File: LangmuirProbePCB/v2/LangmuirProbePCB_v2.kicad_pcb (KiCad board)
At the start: 2 copper layers, 52.5 x 35.5 mm, 10 parts, among them U1 LM741

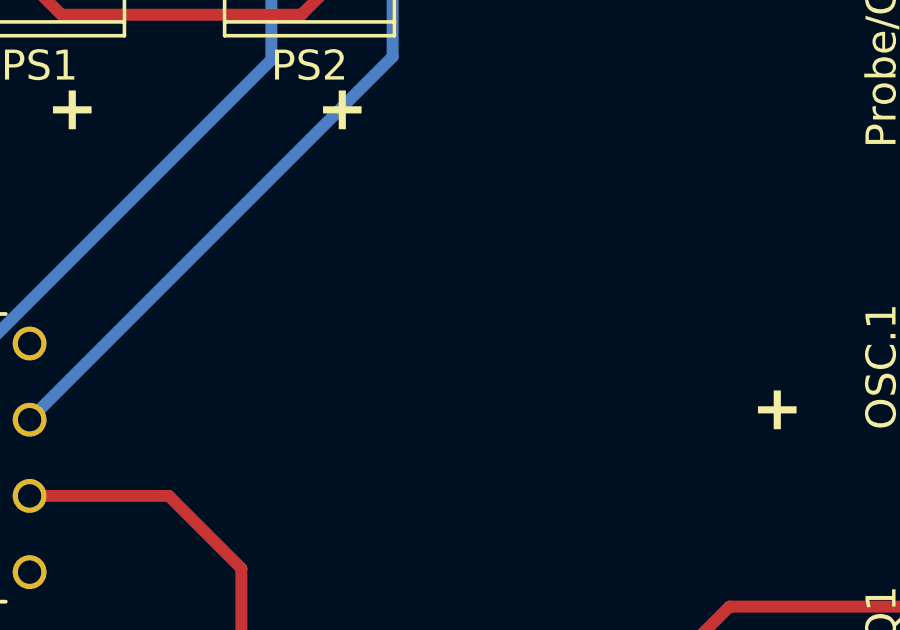
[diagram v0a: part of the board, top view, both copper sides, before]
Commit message: added v3 with OPA454
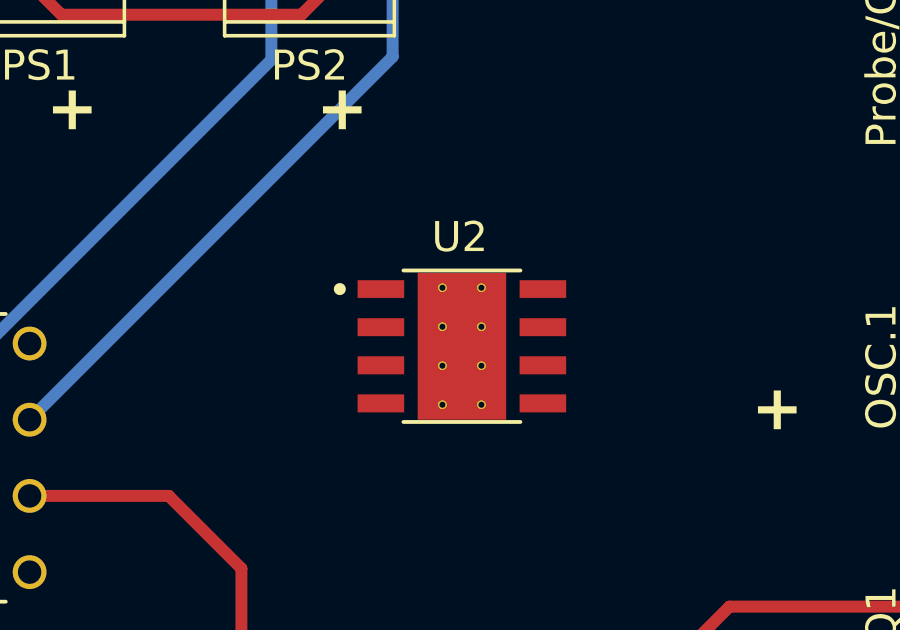
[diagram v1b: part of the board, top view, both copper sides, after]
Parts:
- added U2: OPA454AIDDA, OPA454AIDDA:VREG_LM5017MR_NOPB, F.Cu at (69.8, 49.5)
